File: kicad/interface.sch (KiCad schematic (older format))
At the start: 38 parts, among them J1 BH-10(IDC-10MS), J2 PLS-2, J3 PBD-40(DS1023-2x20), J4 PLD-10(DS1021-2x5), U1 24LC32A/SN, U2 ASEMB-25.000MHZ-LC-T, U3 NUP4114UPXV6T1G, U5 10CL025ZE144, U7 CDCLVC1102PW

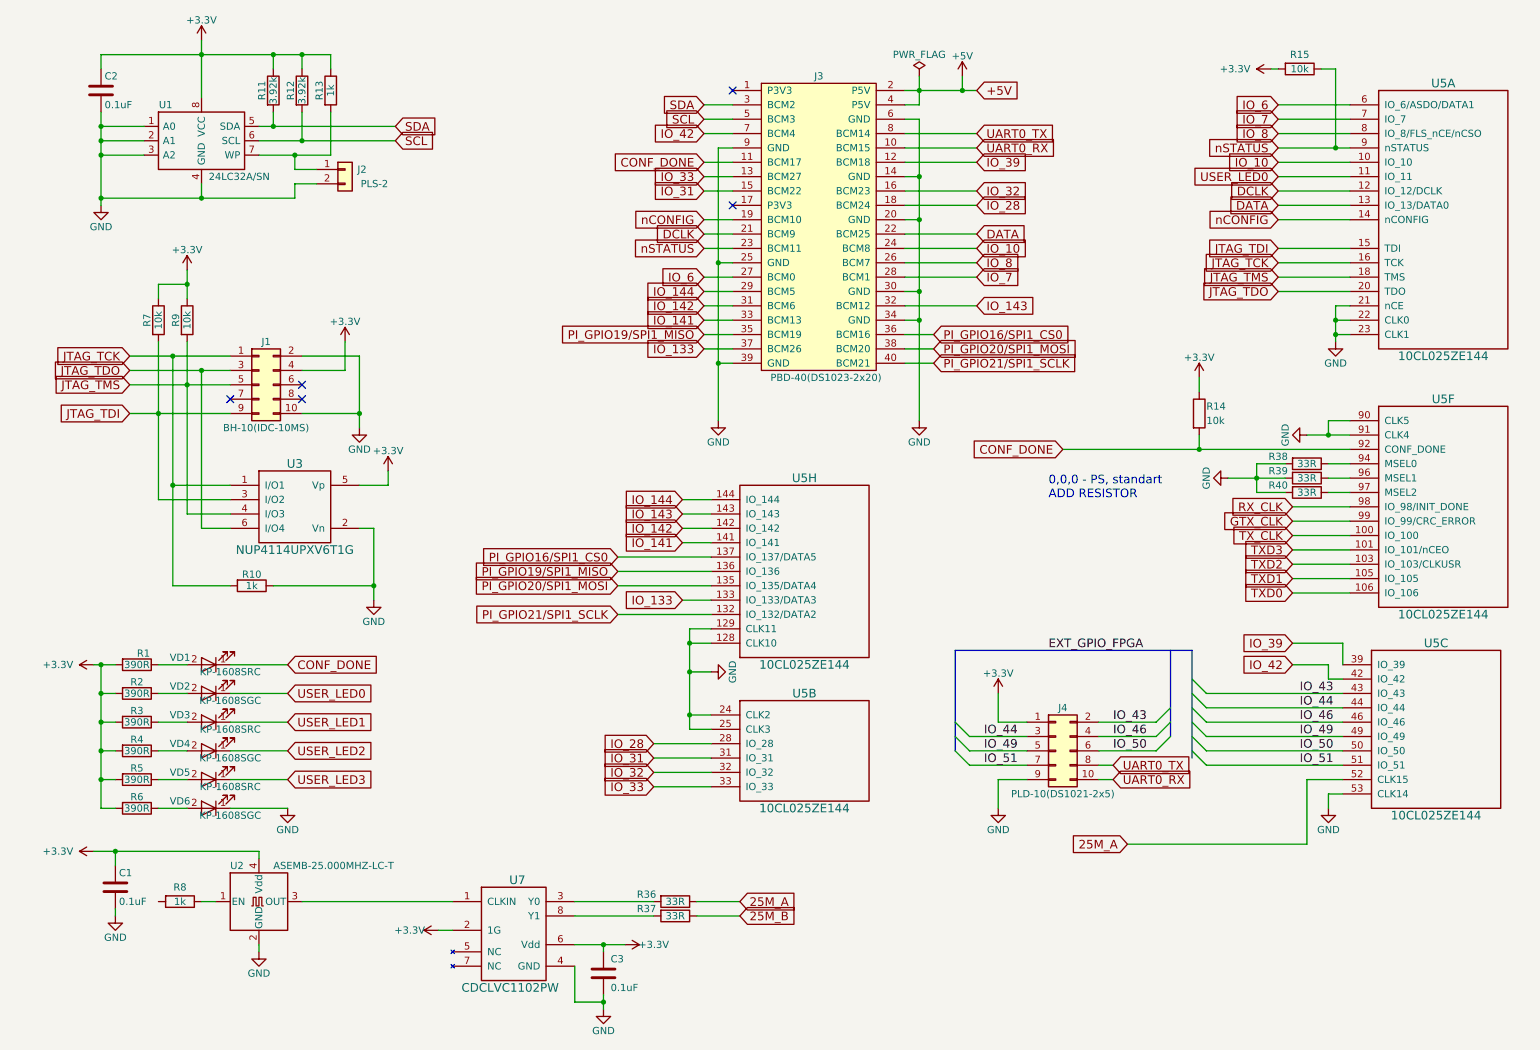
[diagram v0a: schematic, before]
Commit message: Removed footprint for unused components Updated 3d model for LQFP-144 Updated symbol library Updated schematics Updated PCB - finished routing
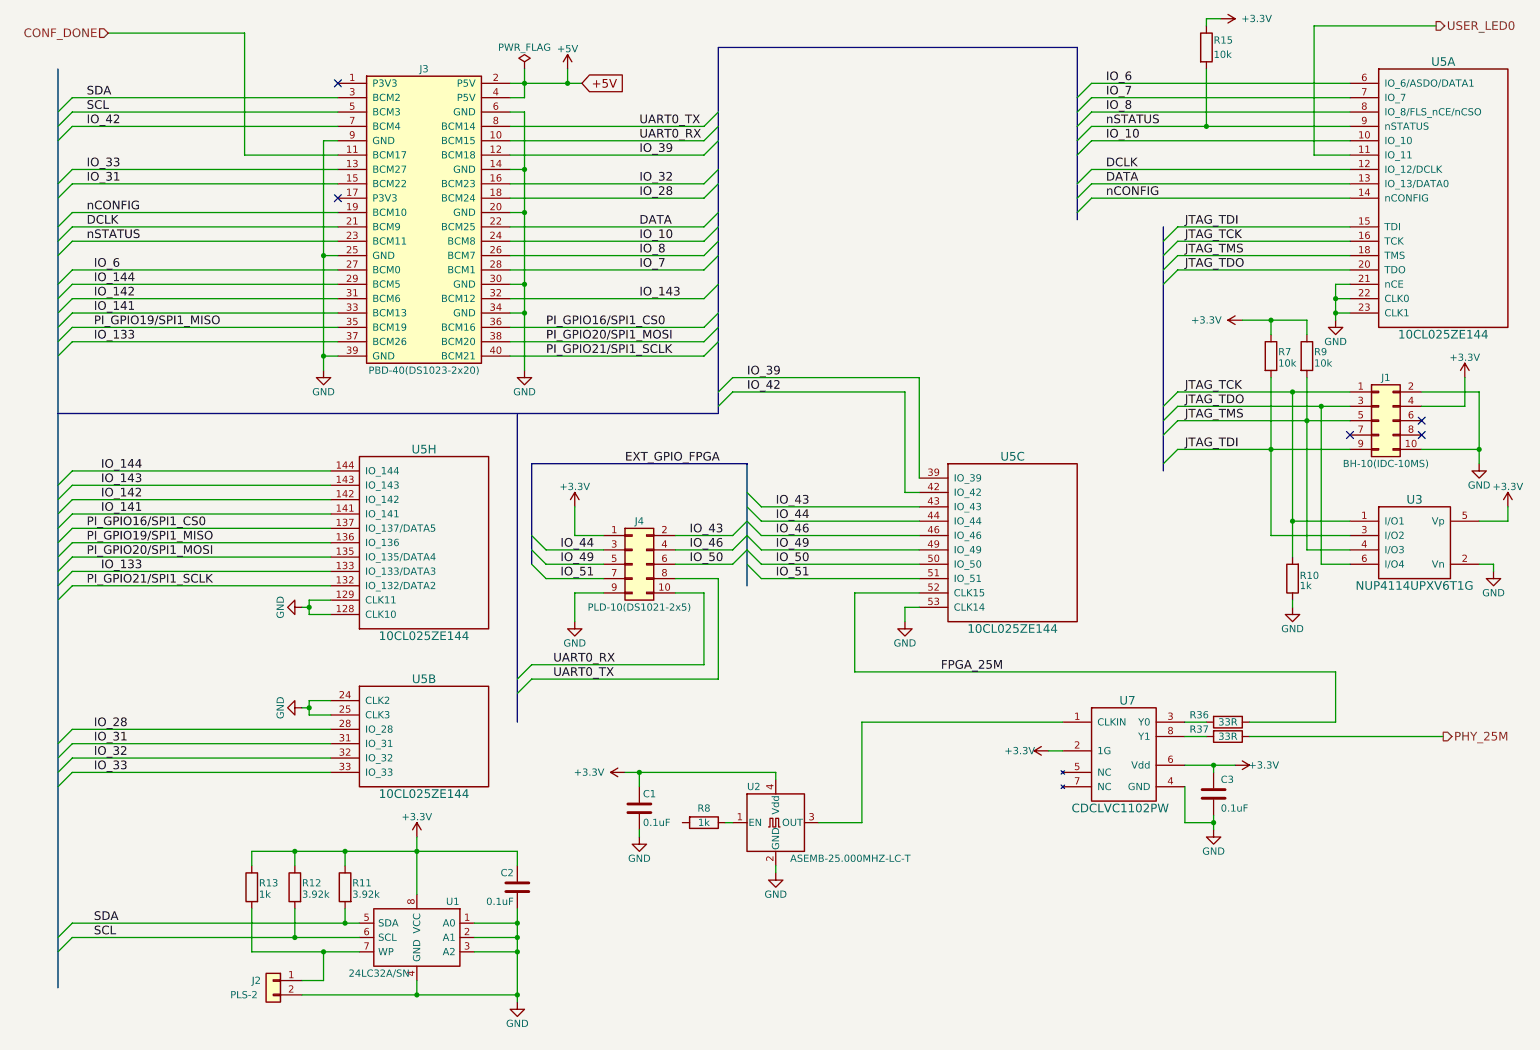
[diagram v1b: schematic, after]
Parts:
- removed J3: PBD-40(DS1023-2x20), Socket_Strips:Socket_Strip_Straight_2x20_Pitch2.54mm, symbol OX40HAT
- removed R1, R2, R3, R4, R5, R6: 390R, Resistors_SMD:R_0603, symbol R
- removed R14: 10k, Resistors_SMD:R_0603, symbol R
- removed R38, R39, R40: 33R, Resistors_SMD:R_0603, symbol R
- removed unit 6 of U5
- removed VD1, VD3, VD5: KP-1608SRC, LEDs:LED_0603, symbol LED
- removed VD2, VD4, VD6: KP-1608SGC, LEDs:LED_0603, symbol LED
- added J3: PBD-40(DS1023-2x20), Socket_Strips:Socket_Strip_Straight_2x20_Pitch2.54mm, symbol Conn_02x20_Odd_Even
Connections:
- net +3V3: now also R15.1; no longer R15.2
- net +5V: now also J3.2 (P5V), J3.4 (P5V)
- net CONF_DONE: now also J3.11 (BCM17)
- net DATA: now also J3.22 (BCM25)
- net DCLK: now also J3.21 (BCM9)
- net GND: now also J3.14 (GND), J3.20 (GND), J3.25 (GND), J3.30 (GND), J3.34 (GND), J3.39 (GND), J3.6 (GND), J3.9 (GND)
- net IO_10: now also J3.24 (BCM8)
- net IO_133: now also J3.37 (BCM26)
- net IO_141: now also J3.33 (BCM13)
- net IO_142: now also J3.31 (BCM6)
- net IO_143: now also J3.32 (BCM12)
- net IO_144: now also J3.29 (BCM5)
- net IO_28: now also J3.18 (BCM24)
- net IO_31: now also J3.15 (BCM22)
- net IO_32: now also J3.16 (BCM23)
- net IO_33: now also J3.13 (BCM27)
- net IO_39: now also J3.12 (BCM18)
- net IO_42: now also J3.7 (BCM4)
- net IO_6: now also J3.27 (BCM0)
- net IO_7: now also J3.28 (BCM1)
- net IO_8: now also J3.26 (BCM7)
- net PI_GPIO16/SPI1_CS0: now also J3.36 (BCM16)
- net PI_GPIO19/SPI1_MISO: now also J3.35 (BCM19)
- net PI_GPIO20/SPI1_MOSI: now also J3.38 (BCM20)
- net PI_GPIO21/SPI1_SCLK: now also J3.40 (BCM21)
- net SCL: now also J3.5 (BCM3)
- net SDA: now also J3.3 (BCM2)
- net UART0_RX: now also J3.10 (BCM15)
- net UART0_TX: now also J3.8 (BCM14)
- net nCONFIG: now also J3.19 (BCM10)
- net nSTATUS: now also R15.2, J3.23 (BCM11); no longer R15.1
- net 25M_A renamed FPGA_25M
- net 25M_B renamed PHY_25M
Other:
- note removed: "0,0,0 - PS, standart\nADD RESISTOR\n"
- moved on the sheet: C1, C2, C3, J1, J2, J4, R10, R11, R12, R13, R15, R36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

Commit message: Add datasheets for new components (Leds, Button, TestPoint) Add 3D models for new components (Leds, Button, TestPoint) Add footprints for new components (Leds, Button, TestPoint) Add new components to schematic library.
Schematic changes:
Change revision 1.0 -> 2.0
Add dual-color and RGB leds. Connect to FPGA.
Add tespoint for GND connection.
Add 2 tactile smd button. Connect to FPGA.
Remove User Gpio Header.
Reconnect FPGA-to-Raspberry connections

PCB changes:
Change revision 1.0 -> 2.0
Rotate RJ-45 connector
Remove text REF around fidusial.
Place new components (Leds, Button, TestPoint)
All connections routed
DRC ok (one error for fidusial)
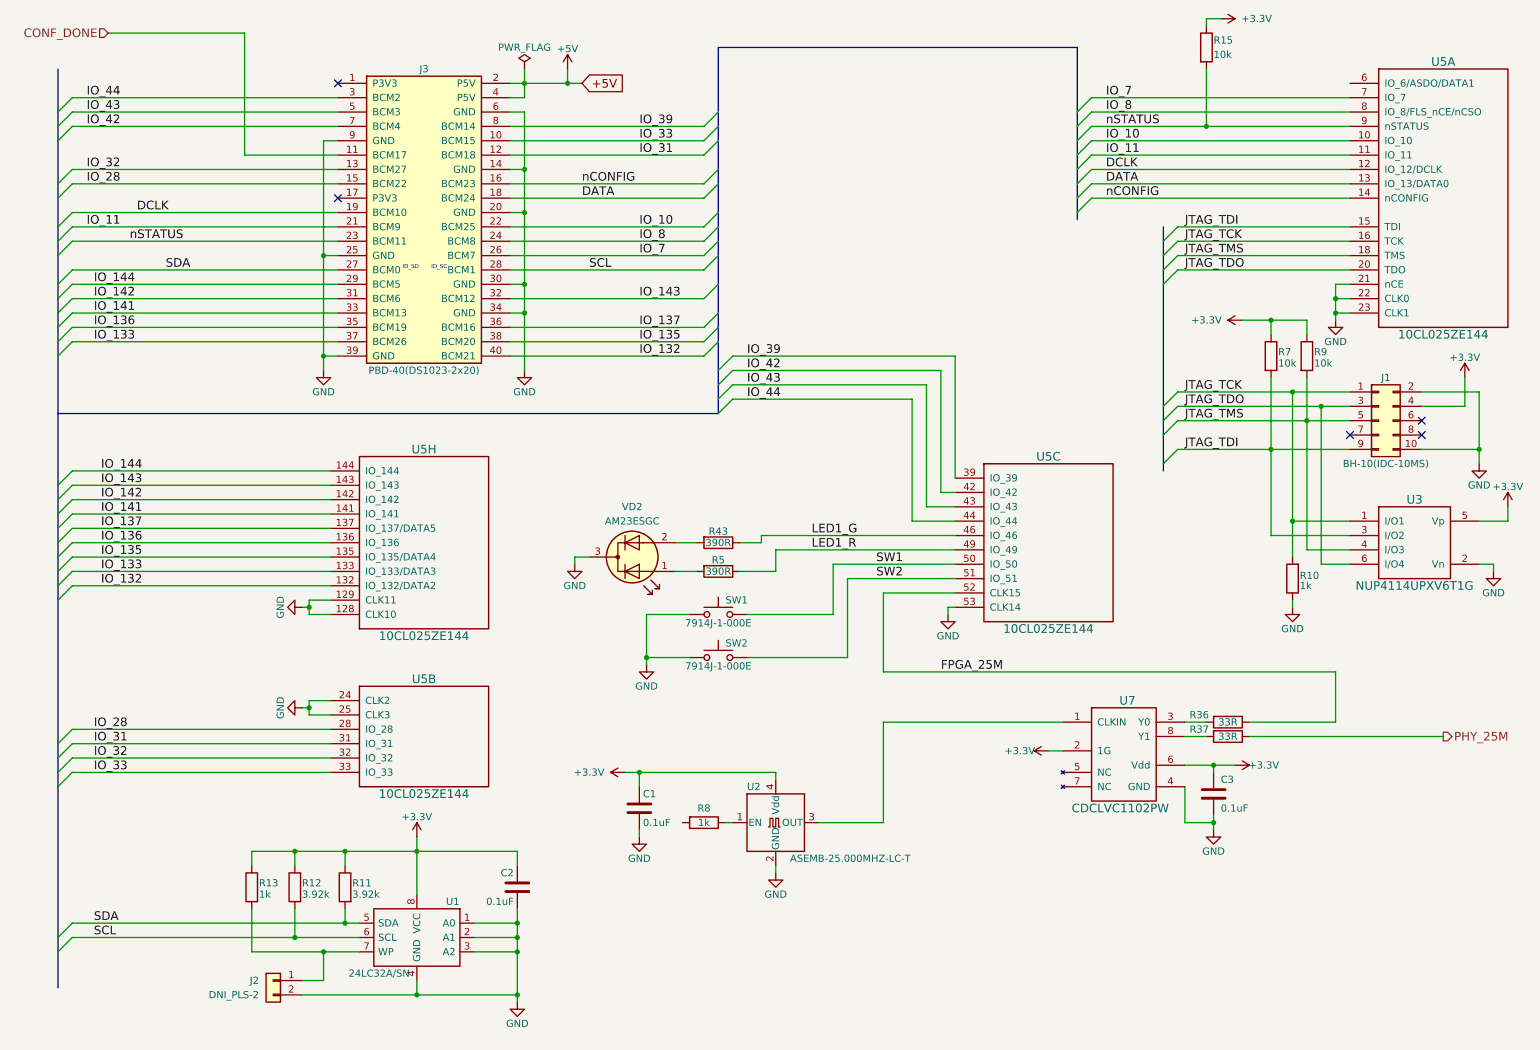
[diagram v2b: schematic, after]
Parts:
- removed J4: PLD-10(DS1021-2x5), Pin_Headers:Pin_Header_Straight_2x05_Pitch2.54mm, symbol Conn_02x05_Odd_Even
- added R43, R5: 390R, Resistors_SMD:R_0603, symbol R
- added SW1, SW2: 7914J-1-000E, project_footprints:7914J-1-000E, symbol SW_Push
- added VD2: AM23ESGC, project_footprints:AM23ESGC, symbol LED_Dual_AAC
- J2: value PLS-2 -> DNI_PLS-2
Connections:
- net UART0_RX is gone; now on net IO_33: J3.10 (BCM15)
- net UART0_TX is gone; now on net IO_39: J3.8 (BCM14)
- net DATA: now also J3.18 (BCM24); no longer J3.22 (BCM25)
- net DCLK: now also J3.19 (BCM10); no longer J3.21 (BCM9)
- net GND: now also SW1.1, SW2.1, VD2.3 (K)
- net IO_10: now also J3.22 (BCM25); no longer J3.24 (BCM8)
- net IO_28: now also J3.15 (BCM22); no longer J3.18 (BCM24)
- net IO_31: now also J3.12 (BCM18); no longer J3.15 (BCM22)
- net IO_32: now also J3.13 (BCM27); no longer J3.16 (BCM23)
- net IO_33: no longer J3.13 (BCM27)
- net IO_39: no longer J3.12 (BCM18)
- net IO_43: now also J3.5 (BCM3)
- net IO_44: now also J3.3 (BCM2)
- net IO_7: now also J3.26 (BCM7); no longer J3.28 (BCM1)
- net IO_8: now also J3.24 (BCM8); no longer J3.26 (BCM7)
- net SCL: now also J3.28 (BCM1); no longer J3.5 (BCM3)
- net SDA: now also J3.27 (BCM0); no longer J3.3 (BCM2)
- net nCONFIG: now also J3.16 (BCM23); no longer J3.19 (BCM10)
- net IO_46 renamed LED1_G
- net LED1_G: now also R43.1
- net IO_49 renamed LED1_R
- net LED1_R: now also R5.1
- net IO_50 renamed SW1
- net SW1: now also SW1.2
- net IO_51 renamed SW2
- net SW2: now also SW2.2
- net IO_6: no longer names the net of U5.6 (IO_6/ASDO/DATA1)
- net IO_6: no longer J3.27 (BCM0)
- net PI_GPIO16/SPI1_CS0 renamed IO_137
- net PI_GPIO19/SPI1_MISO renamed IO_136
- net PI_GPIO20/SPI1_MOSI renamed IO_135
- net PI_GPIO21/SPI1_SCLK renamed IO_132
- net USER_LED0 renamed IO_11
- net IO_11: now also J3.21 (BCM9)
- new net: R5.2, VD2.1 (A1)
- new net: R43.2, VD2.2 (A2)
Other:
- note added: "ID_SC"
- note added: "ID_SD"
- moved on the sheet: U5C
